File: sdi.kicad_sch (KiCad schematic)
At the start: 50 parts, among them J2 031-70526-21, J3 031-70526-21, U11 LIFCL-40-9BG256C, U15 GS2971A, U16 GS2988, Y1 ABM7_27.000MH_D2Y_T

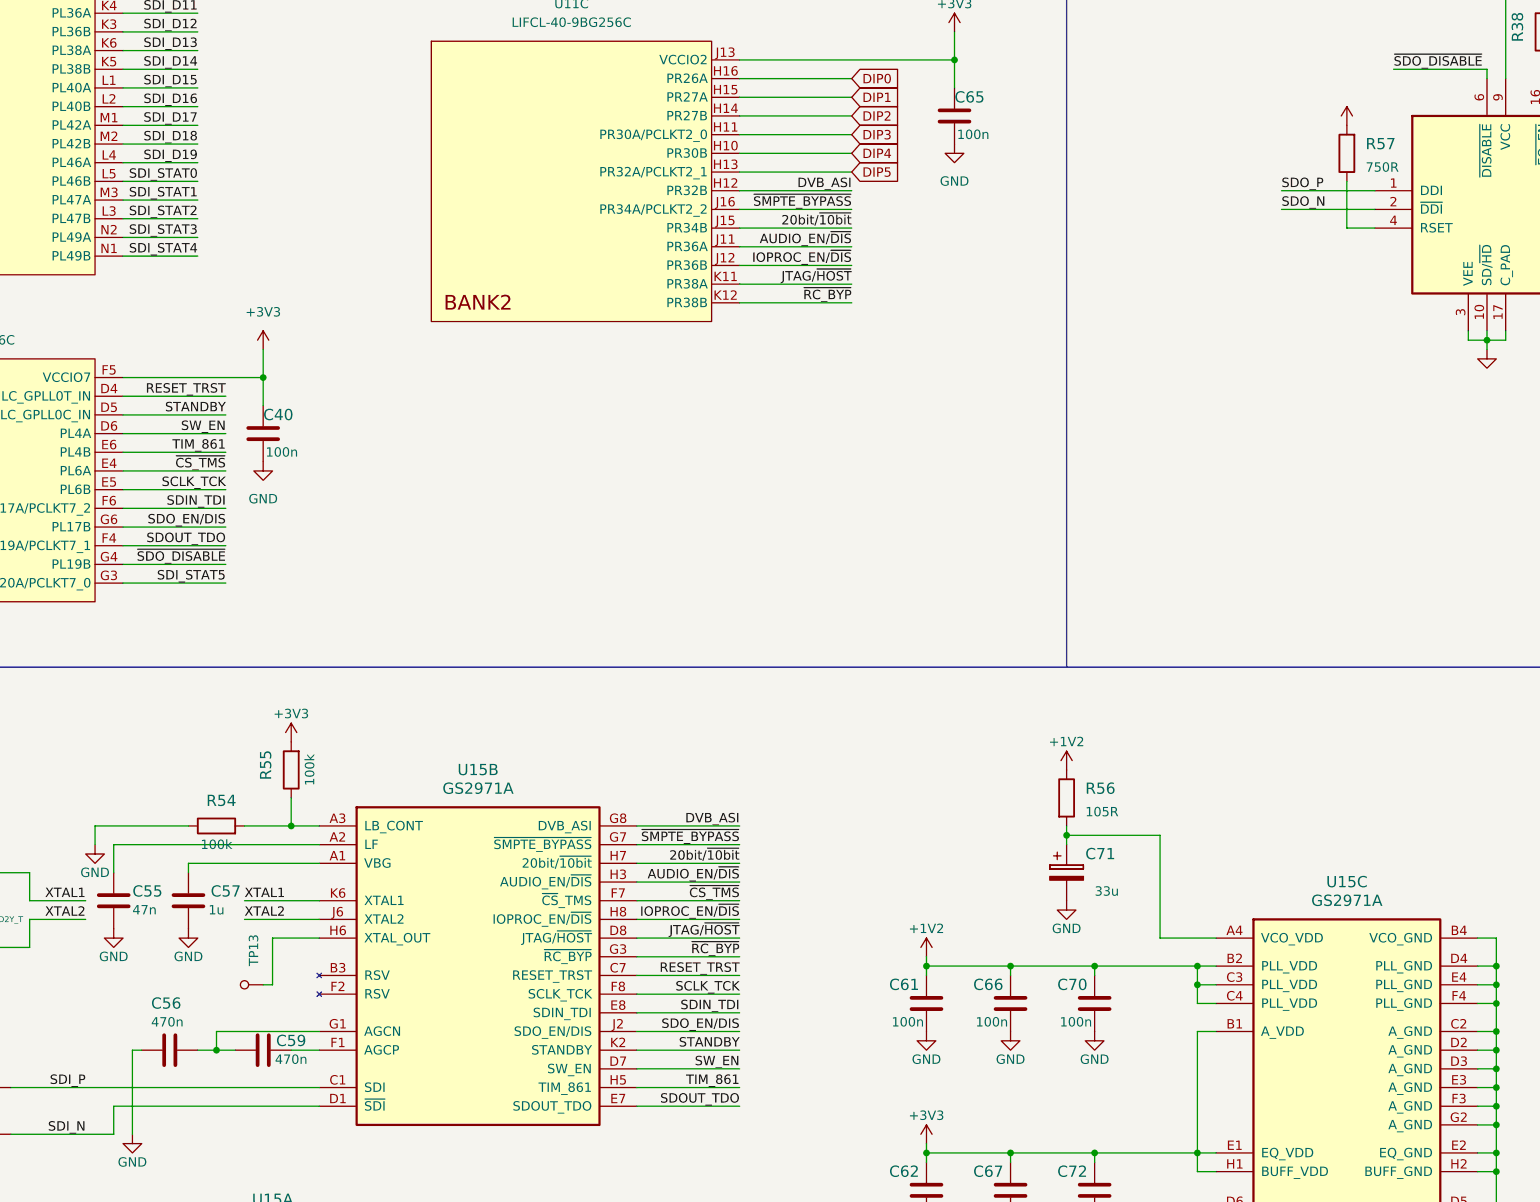
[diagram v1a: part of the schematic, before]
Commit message: Finished component placement
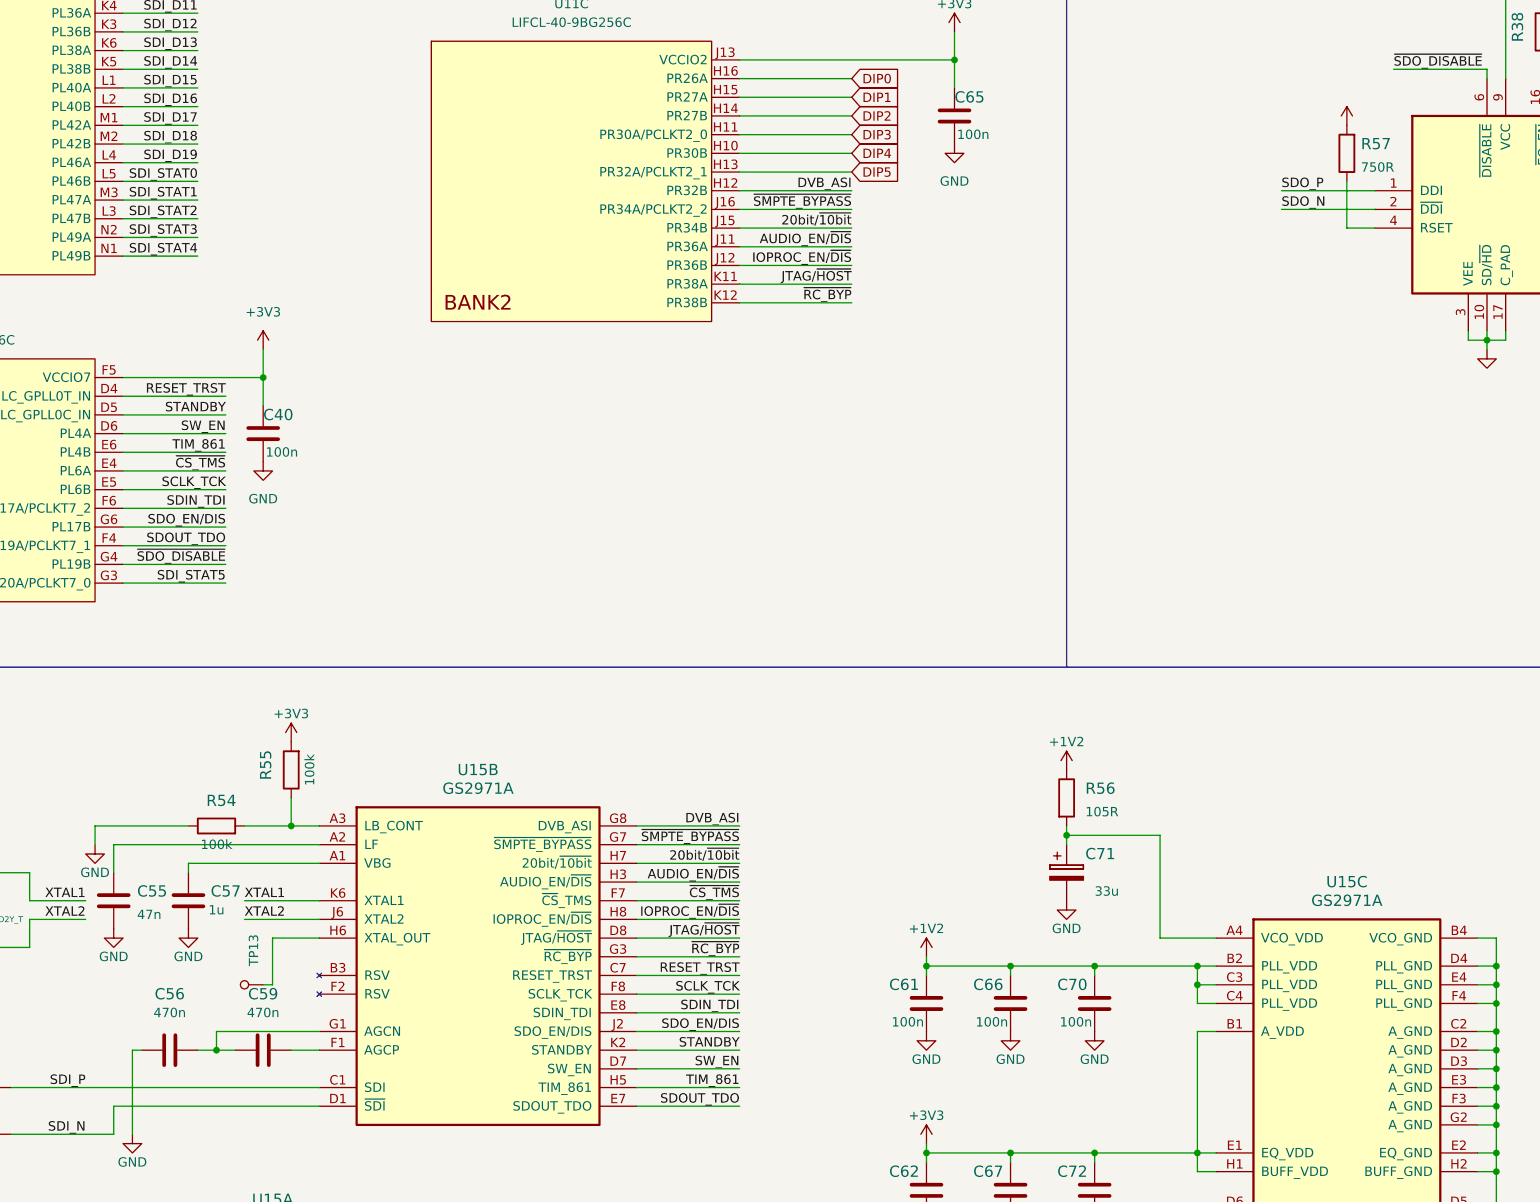
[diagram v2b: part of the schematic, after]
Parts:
- removed C55: C_47n_0603, crosslink-nx-video-converter-footprints:0603-cap, symbol crosslink-nx-video-converter:C_47n_0603
- removed C56, C59: C_470n_0603, crosslink-nx-video-converter-footprints:0603-cap, symbol crosslink-nx-video-converter:C_470n_0603
- removed R57: R_750R_0603, crosslink-nx-video-converter-footprints:0603-res, symbol crosslink-nx-video-converter:R_750R_0603
- added C55: C_47n_0402, antmicro-footprints:0402-cap, symbol antmicroCapacitors0402:C_47n_0402
- added C56, C59: C_470n_0402, antmicro-footprints:0402-cap, symbol antmicroCapacitors0402:C_470n_0402
- added R57: R_750R_0402, antmicro-footprints:0402-res, symbol antmicroResistors0402:R_750R_0402
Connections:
- net +3V3: now also R57.2
- net GND: now also C55.2, C56.1
- net at U15.G1 (AGCN): now also C56.2, C59.1
- net at U15.A2 (LF): now also C55.1
- net at U15.F1 (AGCP): now also C59.2
- net at U16.4 (RSET): now also R57.1
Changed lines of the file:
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@@
+    (pin "2")
+  )
+  (symbol (lib_id "antmicroCapacitors0402:C_470n_0402") (at 115.57 198.12 90) (unit 1)
+    (in_bom yes) (on_board yes) (fields_autoplaced)
+    (property "Reference" "C59" (id 0) (at 115.57 190.5 90)
+      (effects (font (size 1.524 1.524)))
+    )
+    (property "Value" "C_470n_0402" (id 1) (at 119.38 198.12 0)
+      (effects (font (size 1.524 1.524)) hide)
+    )
+    (property "Footprint" "antmicro-footprints:0402-cap" (id 2) (at 110.49 193.04 0)
+      (effects (font (size 1.524 1.524)) (justify left) hide)
+    )
+    (property "Datasheet" "" (id 3) (at 115.57 198.12 0)
+      (effects (font (size 1.27 1.27)) hide)
+    )
+    (property "Manufacturer" "TDK" (id 4) (at 105.41 193.04 0)
+      (effects (font (size 1.524 1.524)) (justify left) hide)
+    )
+    (property "MPN" "C1005X5R1E474M050BB" (id 5) (at 107.95 193.04 0)
+      (effects (font (size 1.524 1.524)) (justify left) hide)
+    )
+    (property "Val" "470n" (id 6) (at 115.57 193.04 90))
+    (pin "1")
     (pin "2")
   )
@@
     (pin "2")
   )
-  (symbol (lib_id "crosslink-nx-video-converter:C_470n_0603") (at 102.87 198.12 270) (unit 1)
-    (in_bom yes) (on_board yes)
-    (property "Reference" "C56" (id 0) (at 100.33 191.77 90)
-      (effects (font (size 1.524 1.524)) (justify left))
-    )
-    (property "Value" "C_470n_0603" (id 1) (at 99.06 198.12 0)
-      (effects (font (size 1.524 1.524)) hide)
-    )
-    (property "Footprint" "crosslink-nx-video-converter-footprints:0603-cap" (id 2) (at 107.95 203.2 0)
-      (effects (font (size 1.524 1.524)) (justify left) hide)
-    )
-    (property "Datasheet" "" (id 3) (at 102.87 198.12 0)
-      (effects (font (size 1.27 1.27)) hide)
-    )
-    (property "Manufacturer" "TDK" (id 4) (at 113.03 203.2 0)
-      (effects (font (size 1.524 1.524)) (justify left) hide)
-    )
-    (property "MPN" "C1608X5R1H474K080AB" (id 5) (at 110.49 203.2 0)
-      (effects (font (size 1.524 1.524)) (justify left) hide)
-    )
-    (property "Val" "470n" (id 6) (at 100.33 194.31 90)
-      (effects (font (size 1.27 1.27)) (justify left))
-    )
-    (pin "1")
-    (pin "2")
-  )
   (symbol (lib_id "power:GND") (at 53.34 187.96 0) (unit 1)
     (in_bom yes) (on_board yes)
@@
     )
     (pin "1")
+  )
+  (symbol (lib_id "antmicroCapacitors0402:C_47n_0402") (at 95.25 177.8 0) (unit 1)
+    (in_bom yes) (on_board yes) (fields_autoplaced)
+    (property "Reference" "C55" (id 0) (at 98.425 176.53 0)
+      (effects (font (size 1.524 1.524)) (justify left))
+    )
+    (property "Value" "C_47n_0402" (id 1) (at 95.25 181.61 0)
+      (effects (font (size 1.524 1.524)) hide)
+    )
+    (property "Footprint" "antmicro-footprints:0402-cap" (id 2) (at 100.33 172.72 0)
+      (effects (font (size 1.524 1.524)) (justify left) hide)
+    )
+    (property "Datasheet" "" (id 3) (at 95.25 177.8 0)
+      (effects (font (size 1.27 1.27)) hide)
+    )
+    (property "Manufacturer" "MULTICOMP" (id 4) (at 100.33 167.64 0)
+      (effects (font (size 1.524 1.524)) (justify left) hide)
+    )
+    (property "MPN" "MC0402X473K160CT" (id 5) (at 100.33 170.18 0)
+      (effects (font (size 1.524 1.524)) (justify left) hide)
+    )
+    (property "Val" "47n" (id 6) (at 98.425 179.7049 0)
+      (effects (font (size 1.27 1.27)) (justify left))
+    )
+    (pin "1")
+    (pin "2")
   )
   (symbol (lib_id "power:GND") (at 391.16 77.47 0) (unit 1)
@@
     (pin "2")
   )
-  (symbol (lib_id "crosslink-nx-video-converter:C_47n_0603") (at 95.25 177.8 0) (unit 1)
-    (in_bom yes) (on_board yes)
-    (property "Reference" "C55" (id 0) (at 97.79 176.53 0)
-      (effects (font (size 1.524 1.524)) (justify left))
-    )
-    (property "Value" "C_47n_0603" (id 1) (at 95.25 181.61 0)
-      (effects (font (size 1.524 1.524)) hide)
-    )
-    (property "Footprint" "crosslink-nx-video-converter-footprints:0603-cap" (id 2) (at 100.33 172.72 0)
-      (effects (font (size 1.524 1.524)) (justify left) hide)
-    )
-    (property "Datasheet" "" (id 3) (at 95.25 177.8 0)
-      (effects (font (size 1.27 1.27)) hide)
-    )
-    (property "Manufacturer" "KEMET" (id 4) (at 100.33 167.64 0)
-      (effects (font (size 1.524 1.524)) (justify left) hide)
-    )
-    (property "MPN" "C0603C473K1RACTU" (id 5) (at 100.33 170.18 0)
-      (effects (font (size 1.524 1.524)) (justify left) hide)
-    )
-    (property "Val" "47n" (id 6) (at 97.79 179.07 0)
-      (effects (font (size 1.27 1.27)) (justify left))
-    )
-    (pin "1")
-    (pin "2")
-  )
   (symbol (lib_id "antmicroCapacitors0402:C_100n_0402") (at 194.31 256.54 0) (unit 1)
     (in_bom yes) (on_board yes)
@@
     (pin "2")
   )
+  (symbol (lib_id "antmicroCapacitors0402:C_470n_0402") (at 102.87 198.12 90) (unit 1)
+    (in_bom yes) (on_board yes) (fields_autoplaced)
+    (property "Reference" "C56" (id 0) (at 102.87 190.5 90)
+      (effects (font (size 1.524 1.524)))
+    )
+    (property "Value" "C_470n_0402" (id 1) (at 106.68 198.12 0)
+      (effects (font (size 1.524 1.524)) hide)
+    )
+    (property "Footprint" "antmicro-footprints:0402-cap" (id 2) (at 97.79 193.04 0)
+      (effects (font (size 1.524 1.524)) (justify left) hide)
+    )
+    (property "Datasheet" "" (id 3) (at 102.87 198.12 0)
+      (effects (font (size 1.27 1.27)) hide)
+    )
+    (property "Manufacturer" "TDK" (id 4) (at 92.71 193.04 0)
+      (effects (font (size 1.524 1.524)) (justify left) hide)
+    )
+    (property "MPN" "C1005X5R1E474M050BB" (id 5) (at 95.25 193.04 0)
+      (effects (font (size 1.524 1.524)) (justify left) hide)
+    )
+    (property "Val" "470n" (id 6) (at 102.87 193.04 90))
+    (pin "1")
+    (pin "2")
+  )
   (symbol (lib_id "crosslink-nx-video-converter:R_75R_0402") (at 55.88 217.17 270) (mirror x) (unit 1)
     (in_bom yes) (on_board yes)
@@
     )
     (pin "1")
-  )
-  (symbol (lib_id "crosslink-nx-video-converter:C_470n_0603") (at 115.57 198.12 90) (unit 1)
-    (in_bom yes) (on_board yes)
-    (property "Reference" "C59" (id 0) (at 119.38 196.85 90)
-      (effects (font (size 1.524 1.524)))
-    )
-    (property "Value" "C_470n_0603" (id 1) (at 119.38 198.12 0)
-      (effects (font (size 1.524 1.524)) hide)
-    )
-    (property "Footprint" "crosslink-nx-video-converter-footprints:0603-cap" (id 2) (at 110.49 193.04 0)
-      (effects (font (size 1.524 1.524)) (justify left) hide)
-    )
-    (property "Datasheet" "" (id 3) (at 115.57 198.12 0)
-      (effects (font (size 1.27 1.27)) hide)
-    )
-    (property "Manufacturer" "TDK" (id 4) (at 105.41 193.04 0)
-      (effects (font (size 1.524 1.524)) (justify left) hide)
-    )
-    (property "MPN" "C1608X5R1H474K080AB" (id 5) (at 107.95 193.04 0)
-      (effects (font (size 1.524 1.524)) (justify left) hide)
-    )
-    (property "Val" "470n" (id 6) (at 119.38 199.39 90))
-    (pin "1")
-    (pin "2")
   )
   (symbol (lib_id "power:+3.3V") (at 119.38 156.21 0) (unit 1)
@@
     (pin "T16")
   )
-  (symbol (lib_id "crosslink-nx-video-converter:R_750R_0603") (at 262.89 76.2 90) (unit 1)
-    (in_bom yes) (on_board yes) (fields_autoplaced)
-    (property "Reference" "R57" (id 0) (at 265.43 74.93 90)
-      (effects (font (size 1.524 1.524)) (justify right))
-    )
-    (property "Value" "R_750R_0603" (id 1) (at 266.7 76.2 0)
-      (effects (font (size 1.524 1.524)) hide)
-    )
-    (property "Footprint" "crosslink-nx-video-converter-footprints:0603-res" (id 2) (at 257.81 71.12 0)
-      (effects (font (size 1.524 1.524)) (justify left) hide)
-    )
-    (property "Datasheet" "" (id 3) (at 262.89 76.2 0)
-      (effects (font (size 1.27 1.27)) hide)
-    )
-    (property "Manufacturer" "TE_CONNECTIVITY_/_NEOHM" (id 4) (at 252.73 71.12 0)
-      (effects (font (size 1.524 1.524)) (justify left) hide)
-    )
-    (property "MPN" "CPF0603F750RC1" (id 5) (at 255.27 71.12 0)
-      (effects (font (size 1.524 1.524)) (justify left) hide)
-    )
-    (property "Val" "750R" (id 6) (at 265.43 78.1049 90)
-      (effects (font (size 1.27 1.27)) (justify right))
-    )
-    (pin "1")
-    (pin "2")
-  )
   (symbol (lib_id "antmicroResistors0402:R_100k_0402") (at 119.38 160.02 90) (unit 1)
     (in_bom yes) (on_board yes)
@@
     (pin "1")
     (pin "2")
+  )
+  (symbol (lib_id "antmicroResistors0402:R_750R_0402") (at 262.89 76.2 90) (unit 1)
+    (in_bom yes) (on_board yes) (fields_autoplaced)
+    (property "Reference" "R57" (id 0) (at 264.795 74.93 90)
+      (effects (font (size 1.524 1.524)) (justify right))
+    )
+    (property "Value" "R_750R_0402" (id 1) (at 266.7 76.2 0)
+      (effects (font (size 1.524 1.524)) hide)
+    )
+    (property "Footprint" "antmicro-footprints:0402-res" (id 2) (at 257.81 71.12 0)
+      (effects (font (size 1.524 1.524)) (justify left) hide)
+    )
+    (property "Datasheet" "" (id 3) (at 262.89 76.2 0)
+      (effects (font (size 1.27 1.27)) hide)
+    )
+    (property "Manufacturer" "Yageo" (id 4) (at 252.73 71.12 0)
+      (effects (font (size 1.524 1.524)) (justify left) hide)
+    )
+    (property "MPN" "RC0402FR-07750RL" (id 5) (at 255.27 71.12 0)
+      (effects (font (size 1.524 1.524)) (justify left) hide)
+    )
+    (property "Val" "750R" (id 6) (at 264.795 78.1049 90)
+      (effects (font (size 1.27 1.27)) (justify right))
+    )
+    (pin "1")
+    (pin "2")

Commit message: Loclib
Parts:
- C40, C58, C60, C61, C62, C63, C64, C65, C66, C67, C68, C69, C70, C72, C73, C74: footprint antmicro-footprints:0402-cap -> crosslink-nx-video-converter-footprints:0402-cap; symbol antmicroCapacitors0402:C_100n_0402 -> crosslink-nx-video-converter:C_100n_0402
- C51, C52: footprint antmicro-footprints:0402-cap -> crosslink-nx-video-converter-footprints:0402-cap; symbol antmicroCapacitors0402:C_33p_0402 -> crosslink-nx-video-converter:C_33p_0402
- C55: footprint antmicro-footprints:0402-cap -> crosslink-nx-video-converter-footprints:0402-cap; symbol antmicroCapacitors0402:C_47n_0402 -> crosslink-nx-video-converter:C_47n_0402
- C56, C59: footprint antmicro-footprints:0402-cap -> crosslink-nx-video-converter-footprints:0402-cap; symbol antmicroCapacitors0402:C_470n_0402 -> crosslink-nx-video-converter:C_470n_0402
- R38: footprint antmicro-footprints:0402-res -> crosslink-nx-video-converter-footprints:0402-res; symbol antmicroResistors0402:R_0R_0402 -> crosslink-nx-video-converter:R_0R_0402
- R54, R55: footprint antmicro-footprints:0402-res -> crosslink-nx-video-converter-footprints:0402-res; symbol antmicroResistors0402:R_100k_0402 -> crosslink-nx-video-converter:R_100k_0402
- R57: footprint antmicro-footprints:0402-res -> crosslink-nx-video-converter-footprints:0402-res; symbol antmicroResistors0402:R_750R_0402 -> crosslink-nx-video-converter:R_750R_0402
- TP13, TP14: footprint antmicro-footprints:Testpoint_smd_0_75mm -> crosslink-nx-video-converter-footprints:Testpoint_smd_0_75mm; symbol antmicroTestPoints:TP_SMD_0_75MM -> crosslink-nx-video-converter:TP_SMD_0_75MM
- U11: footprint antmicro-footprints:BGA-256_16x16_14.0x14.0mm -> crosslink-nx-video-converter-footprints:BGA-256_16x16_14.0x14.0mm; symbol antmicroBGAchips:LIFCL-40-9BG256C -> crosslink-nx-video-converter:LIFCL-40-9BG256C
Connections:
- net +3V3: no longer U11.F5 (VCCIO7), U11.J4 (VCCIO6)
- net RESET_TRST: no longer U11.D4 (PL3A/ULC_GPLL0T_IN)
- net SCLK_TCK: no longer U11.E5 (PL6B)
- net SDIN_TDI: no longer U11.F6 (PL17A/PCLKT7_2)
- net SDI_D0: no longer U11.H6 (PL24A)
- net SDI_D1: no longer U11.H5 (PL24B)
- net SDI_D10: no longer U11.K2 (PL34B)
- net SDI_D11: no longer U11.K4 (PL36A)
- net SDI_D12: no longer U11.K3 (PL36B)
- net SDI_D13: no longer U11.K6 (PL38A)
- net SDI_D14: no longer U11.K5 (PL38B)
- net SDI_D15: no longer U11.L1 (PL40A)
- net SDI_D16: no longer U11.L2 (PL40B)
- net SDI_D17: no longer U11.M1 (PL42A)
- net SDI_D18: no longer U11.M2 (PL42B)
- net SDI_D19: no longer U11.L4 (PL46A)
- net SDI_D2: no longer U11.H4 (PL26A)
- net SDI_D3: no longer U11.H3 (PL26B)
- net SDI_D4: no longer U11.H1 (PL27A)
- net SDI_D5: no longer U11.H2 (PL27B)
- net SDI_D6: no longer U11.J5 (PL30B)
- net SDI_D7: no longer U11.J1 (PL32A/PCLKT6_1)
- net SDI_D8: no longer U11.J2 (PL32B)
- net SDI_D9: no longer U11.K1 (PL34A/PCLKT6_2)
- net SDI_PCLK: no longer U11.J6 (PL30A/PCLKT6_0)
- net SDI_STAT0: no longer U11.L5 (PL46B)
- net SDI_STAT1: no longer U11.M3 (PL47A)
- net SDI_STAT2: no longer U11.L3 (PL47B)
- net SDI_STAT3: no longer U11.N2 (PL49A)
- net SDI_STAT4: no longer U11.N1 (PL49B)
- net SDI_STAT5: no longer U11.G3 (PL20A/PCLKT7_0)
- net SDOUT_TDO: no longer U11.F4 (PL19A/PCLKT7_1)
- net SDO_EN/DIS: no longer U11.G6 (PL17B)
- net STANDBY: no longer U11.D5 (PL3B/ULC_GPLL0C_IN)
- net SW_EN: no longer U11.D6 (PL4A)
- net TIM_861: no longer U11.E6 (PL4B)
- net ~{CS_TMS}: no longer U11.E4 (PL6A)
- net ~{SDO_DISABLE}: no longer U11.G4 (PL19B)

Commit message: Routed hard CSI
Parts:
- removed unit 8 of U11
- removed unit 7 of U11
- added unit 8 of U11
- added unit 7 of U11
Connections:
- net +3V3: now also U11.F5 (VCCIO7), U11.J4 (VCCIO6)
- net RESET_TRST: now also U11.D4 (PL3A/ULC_GPLL0T_IN)
- net SCLK_TCK: now also U11.E5 (PL6B)
- net SDIN_TDI: now also U11.F6 (PL17A/PCLKT7_2)
- net SDI_D0: now also U11.H6 (PL24A)
- net SDI_D1: now also U11.H5 (PL24B)
- net SDI_D10: now also U11.K2 (PL34B)
- net SDI_D11: now also U11.K4 (PL36A)
- net SDI_D12: now also U11.K3 (PL36B)
- net SDI_D13: now also U11.K6 (PL38A)
- net SDI_D14: now also U11.K5 (PL38B)
- net SDI_D15: now also U11.L1 (PL40A)
- net SDI_D16: now also U11.L2 (PL40B)
- net SDI_D17: now also U11.M1 (PL42A)
- net SDI_D18: now also U11.M2 (PL42B)
- net SDI_D19: now also U11.L4 (PL46A)
- net SDI_D2: now also U11.H4 (PL26A)
- net SDI_D3: now also U11.H3 (PL26B)
- net SDI_D4: now also U11.H1 (PL27A)
- net SDI_D5: now also U11.H2 (PL27B)
- net SDI_D6: now also U11.J5 (PL30B)
- net SDI_D7: now also U11.J1 (PL32A/PCLKT6_1)
- net SDI_D8: now also U11.J2 (PL32B)
- net SDI_D9: now also U11.K1 (PL34A/PCLKT6_2)
- net SDI_PCLK: now also U11.J6 (PL30A/PCLKT6_0)
- net SDI_STAT0: now also U11.L5 (PL46B)
- net SDI_STAT1: now also U11.M3 (PL47A)
- net SDI_STAT2: now also U11.L3 (PL47B)
- net SDI_STAT3: now also U11.N2 (PL49A)
- net SDI_STAT4: now also U11.N1 (PL49B)
- net SDI_STAT5: now also U11.G3 (PL20A/PCLKT7_0)
- net SDOUT_TDO: now also U11.F4 (PL19A/PCLKT7_1)
- net SDO_EN/DIS: now also U11.G6 (PL17B)
- net STANDBY: now also U11.D5 (PL3B/ULC_GPLL0C_IN)
- net SW_EN: now also U11.D6 (PL4A)
- net TIM_861: now also U11.E6 (PL4B)
- net ~{CS_TMS}: now also U11.E4 (PL6A)
- net ~{SDO_DISABLE}: now also U11.G4 (PL19B)
